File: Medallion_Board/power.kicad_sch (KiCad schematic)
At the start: 19 parts, among them Q1 DMG3415U, U3 RT9080-33GJ5, U4 MCP73831T-2ACI_OT, U5 MAX17048G_T10

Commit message: Some minor cleaning
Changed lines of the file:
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@@
 		(title "Smart Compass")
 		(date "2026-06-04")
+		(rev "0.2")
 	)
 	(rectangle
@@
 		(property "Value" "GND"
 			(at 74.93 97.79 0)
+			(hide yes)
 			(show_name no)
 			(do_not_autoplace no)
@@
 		(property "Value" "GND"
 			(at 170.18 76.2 0)
+			(hide yes)
 			(show_name no)
 			(do_not_autoplace no)
@@
 		(property "Value" "GND"
 			(at 147.32 76.2 0)
+			(hide yes)
 			(show_name no)
 			(do_not_autoplace no)
@@
 		(property "Value" "GND"
 			(at 88.9 134.62 0)
+			(hide yes)
 			(show_name no)
 			(do_not_autoplace no)
@@
 		(property "Value" "GND"
 			(at 36.83 74.93 0)
+			(hide yes)
 			(show_name no)
 			(do_not_autoplace no)
@@
 		(property "Value" "GND"
 			(at 30.48 123.19 0)
+			(hide yes)
 			(show_name no)
 			(do_not_autoplace no)
@@
 		(property "Value" "GND"
 			(at 207.01 80.01 0)
+			(hide yes)
 			(show_name no)
 			(do_not_autoplace no)
@@
 		(property "Value" "GND"
 			(at 177.8 76.2 0)
+			(hide yes)
 			(show_name no)
 			(do_not_autoplace no)
@@
 		(property "Value" "GND"
 			(at 156.21 49.53 0)
+			(hide yes)
 			(show_name no)
 			(do_not_autoplace no)
@@
 		(property "Value" "GND"
 			(at 101.6 72.39 0)
+			(hide yes)
 			(show_name no)
 			(do_not_autoplace no)
@@
 		(property "Value" "GND"
 			(at 135.89 76.2 0)
+			(hide yes)
 			(show_name no)
 			(do_not_autoplace no)
@@
 		(property "Value" "GND"
 			(at 116.84 76.2 0)
+			(hide yes)
 			(show_name no)
 			(do_not_autoplace no)
@@
 		(property "Value" "GND"
 			(at 182.88 54.61 0)
+			(hide yes)
 			(show_name no)
 			(do_not_autoplace no)

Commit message: review bom and footprints
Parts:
- ONOFF1: Check_prices https://www.snapeda.com/parts/SM02B-GHS-TB/JST/view-part/?r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 -> (none); Package None -> (none); SnapEDA_Link https://www.snapeda.com/parts/SM02B-GHS-TB/JST/view-part/?r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 -> (none)
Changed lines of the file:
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@@
-			)
-		)
-		(property "SnapEDA_Link" "https://www.snapeda.com/parts/SM02B-GHS-TB/JST/view-part/?ref=snap"
-			(at 166.37 41.91 0)
-			(hide yes)
-			(show_name no)
-			(do_not_autoplace no)
-			(effects
-				(font
-					(size 1.27 1.27)
-				)
-				(justify bottom)
-			)
-		)
-		(property "Package" "None"
-			(at 166.37 41.91 0)
-			(hide yes)
-			(show_name no)
-			(do_not_autoplace no)
-			(effects
-				(font
-					(size 1.27 1.27)
-				)
-				(justify bottom)
-			)
-		)
-		(property "Check_prices" "https://www.snapeda.com/parts/SM02B-GHS-TB/JST/view-part/?ref=eda"
-			(at 166.37 41.91 0)
-			(hide yes)
-			(show_name no)
-			(do_not_autoplace no)
-			(effects
-				(font
-					(size 1.27 1.27)
-				)
-				(justify bottom)
 			)
 		)

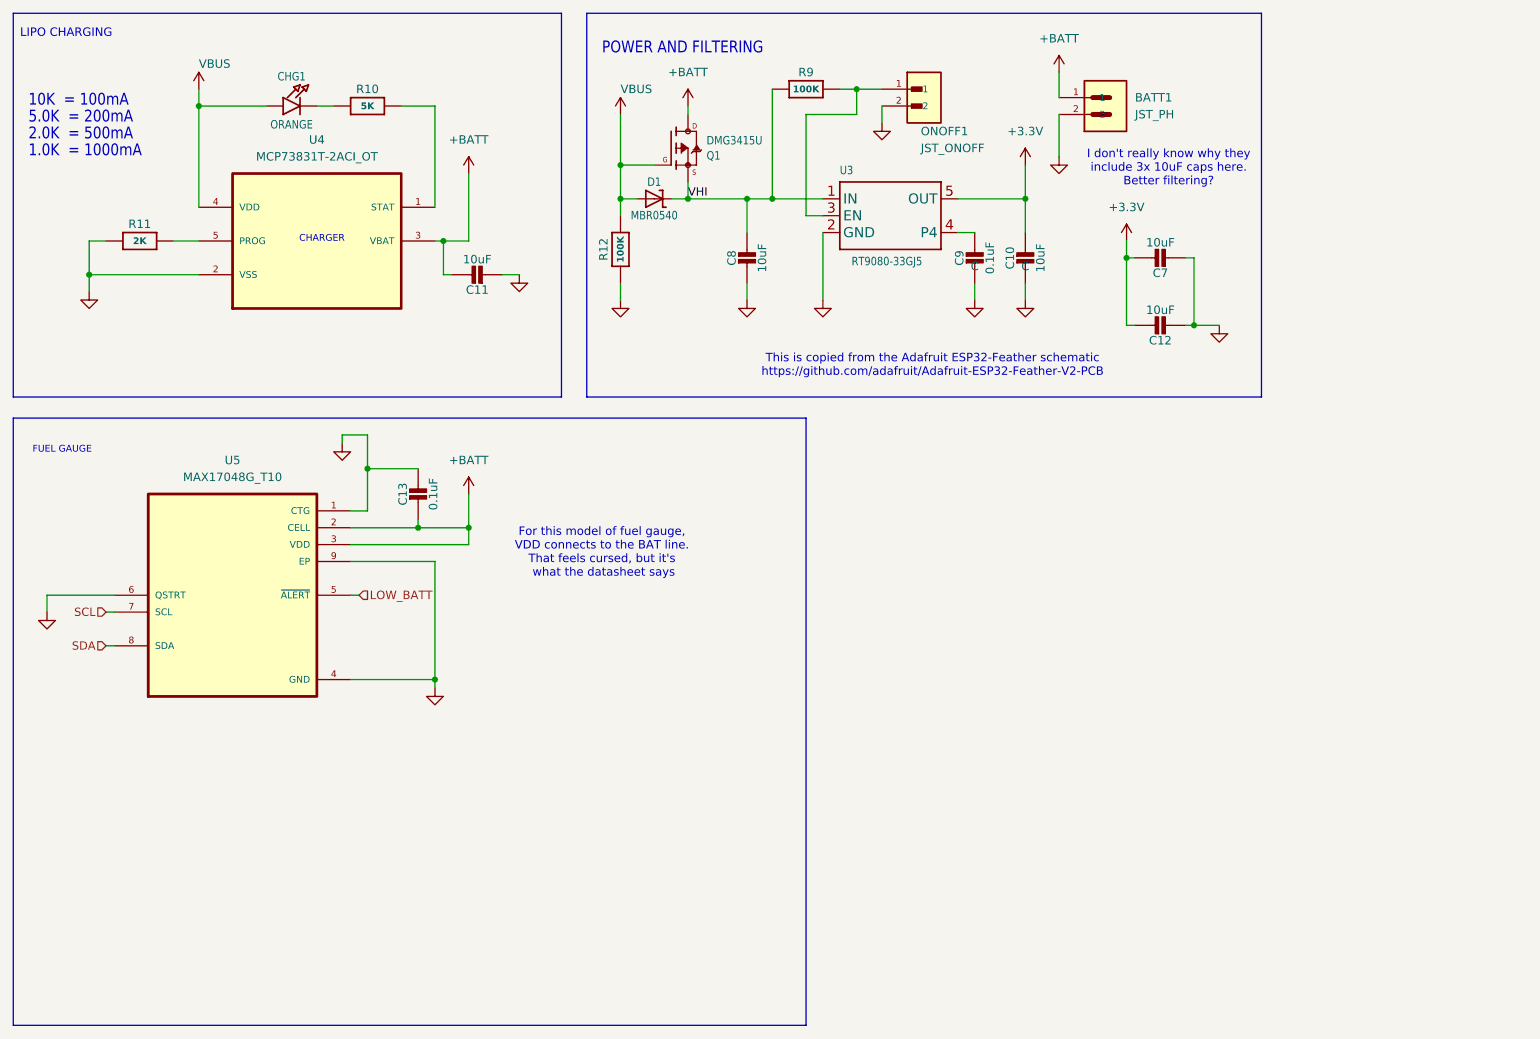
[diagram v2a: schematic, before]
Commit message: Re-did the layout and routing for the whole board. Added more LEDs, haptics, and properly modelled the e-ink display
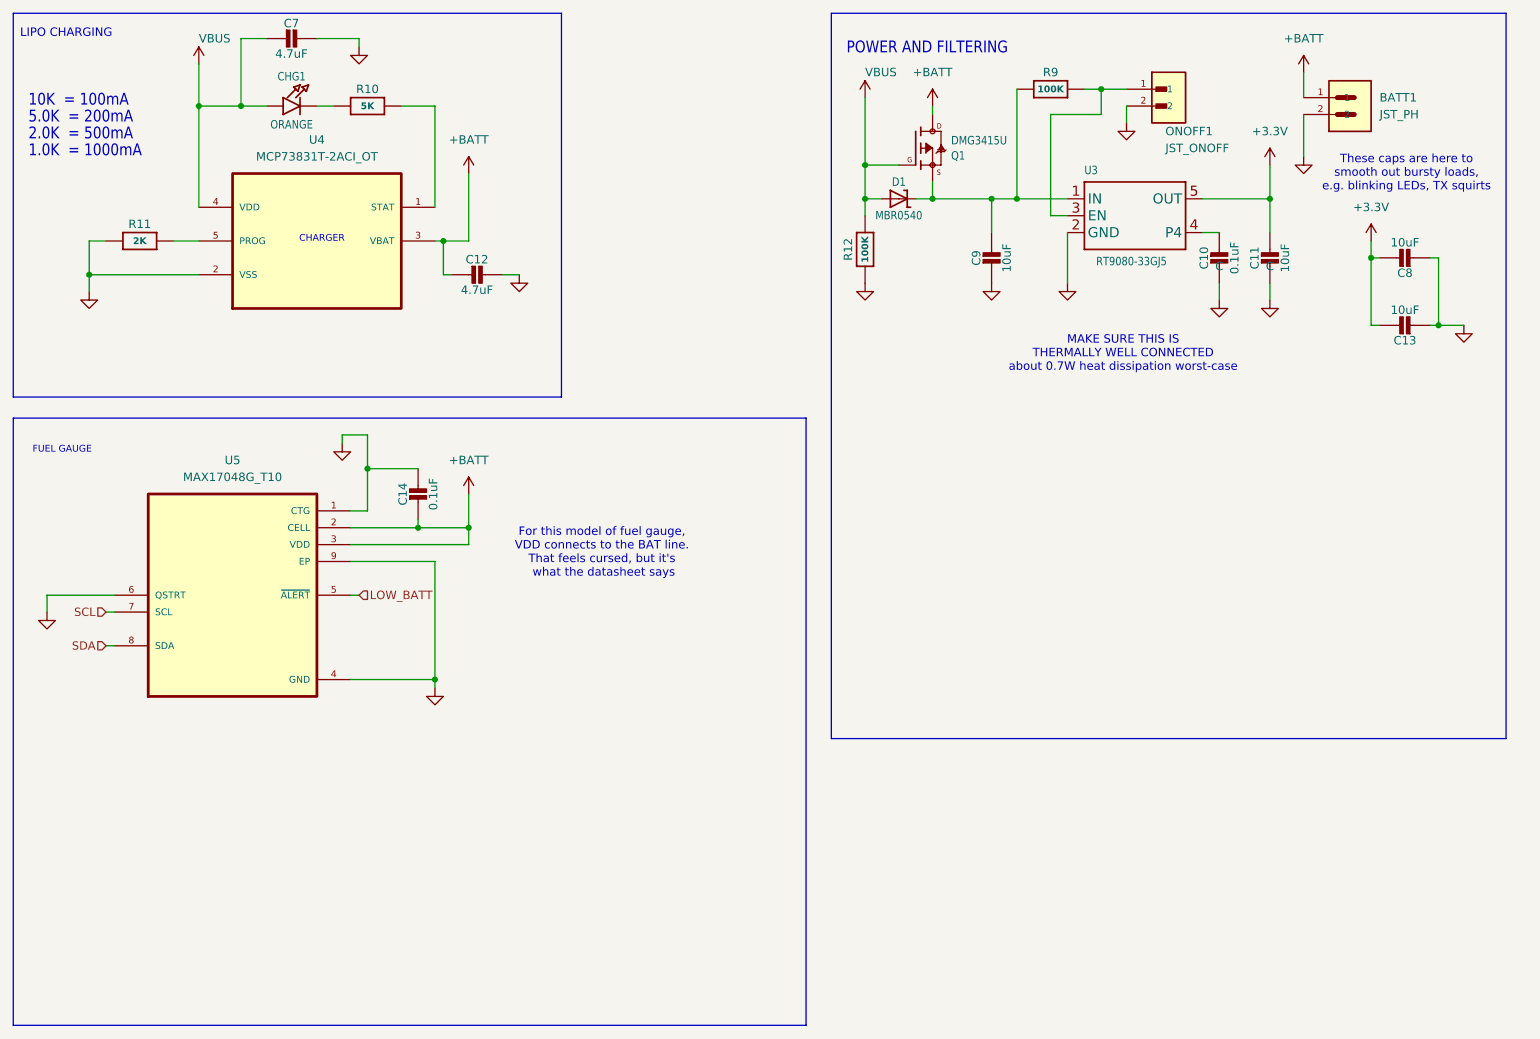
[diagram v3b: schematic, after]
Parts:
- removed C11: 10uF, Capacitor_SMD:C_0805_2012Metric, symbol Adafruit ESP32-S3 8MB No PSRAM-eagle-import:CAP_CERAMIC0805-NOOUTLINE
- added C12, C7: 4.7uF, Capacitor_SMD:C_0402_1005Metric, symbol Adafruit ESP32-S3 8MB No PSRAM-eagle-import:CAP_CERAMIC0603_NO
- U5: PRICE 4.22 -> 3.13
- renumbered C9 to C10, C10 to C11, C12 to C13, C13 to C14, C7 to C8, C8 to C9
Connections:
- net +BATT: now also C12.2
- net GND: now also C12.1, C7.1
- net VBUS: now also C7.2
- net VHI: no longer names the net of C9.1, D1.2, Q1.2 (S), R9.1, U3.1 (IN)
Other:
- note added: "MAKE SURE THIS IS THERMALLY WELL CONNECTED about 0.7W heat dissipation worst-case"
- note added: "These caps are here to smooth out bursty loads, e.g. blinking LEDs, TX squirts"
- note removed: "I don't really know why they include 3x 10uF caps here. Better filtering?"
- note removed: "This is copied from the Adafruit ESP32-Feather schematic https://github.com/adafruit/Adafruit-ESP32-Feather-V2-PCB"
- moved on the sheet: BATT1, C10, C11, C13, C8, C9, D1, ONOFF1, Q1, R12, R9, U3
